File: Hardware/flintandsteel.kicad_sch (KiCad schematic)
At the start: 41 parts, among them J1 RBUS, U1 ESP32-S3, Y1 40MHz±10ppm

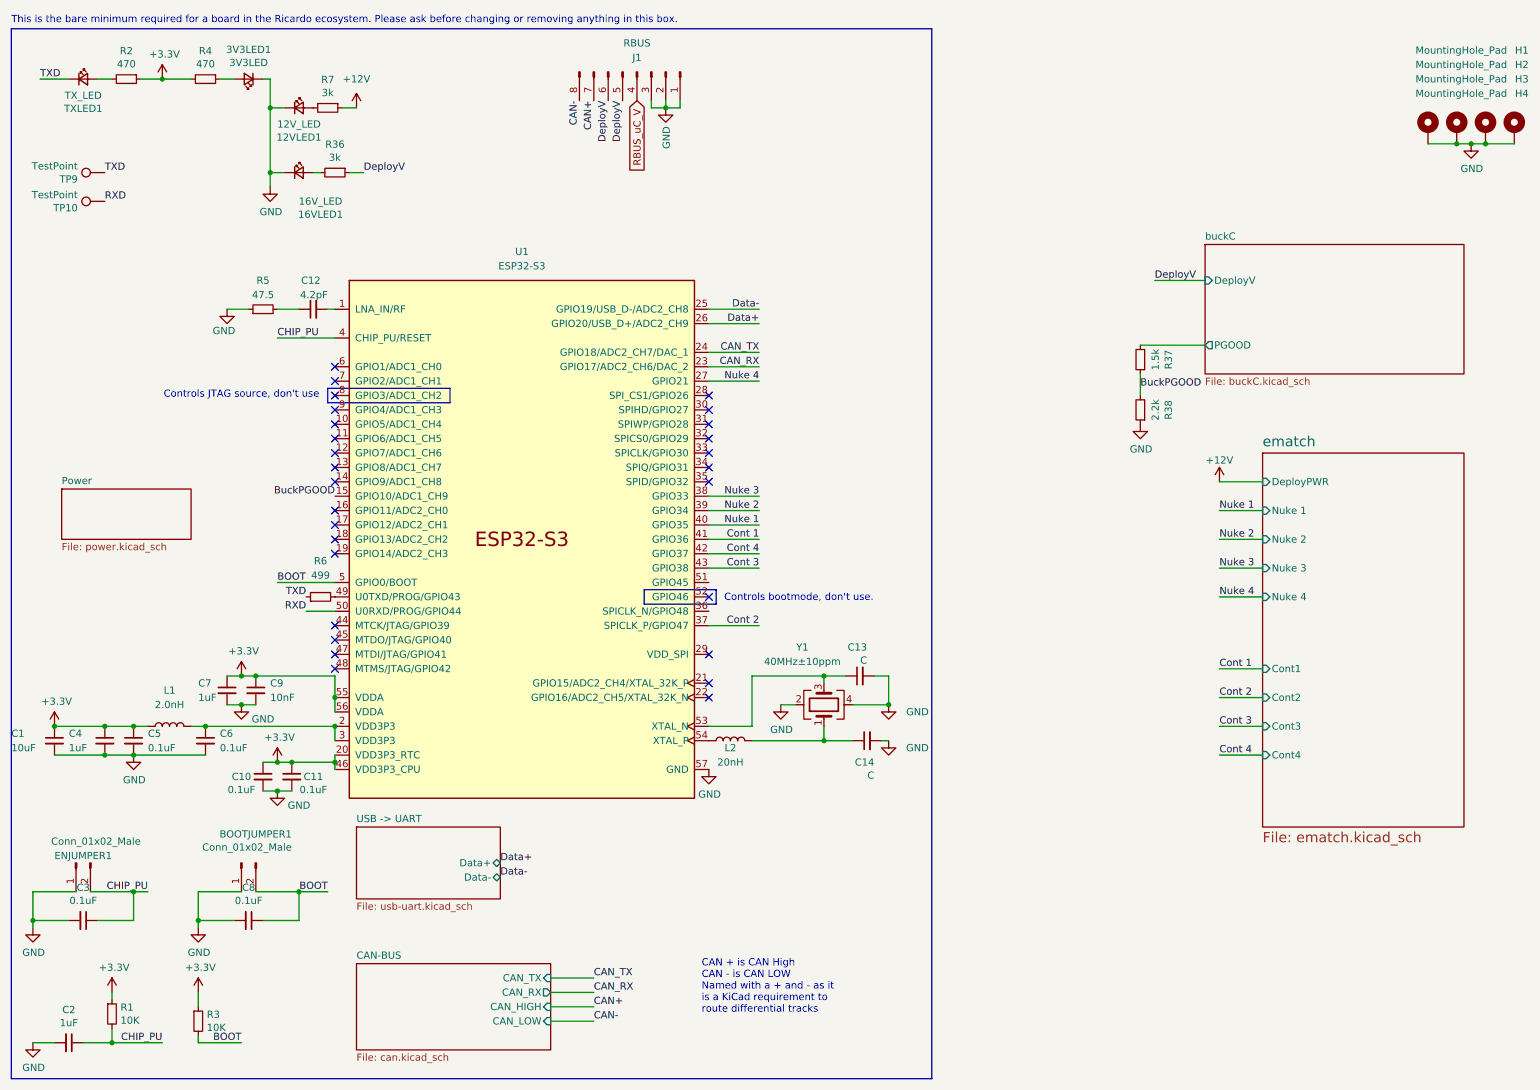
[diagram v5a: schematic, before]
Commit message: no buck, technically complete but I still want to make some changes
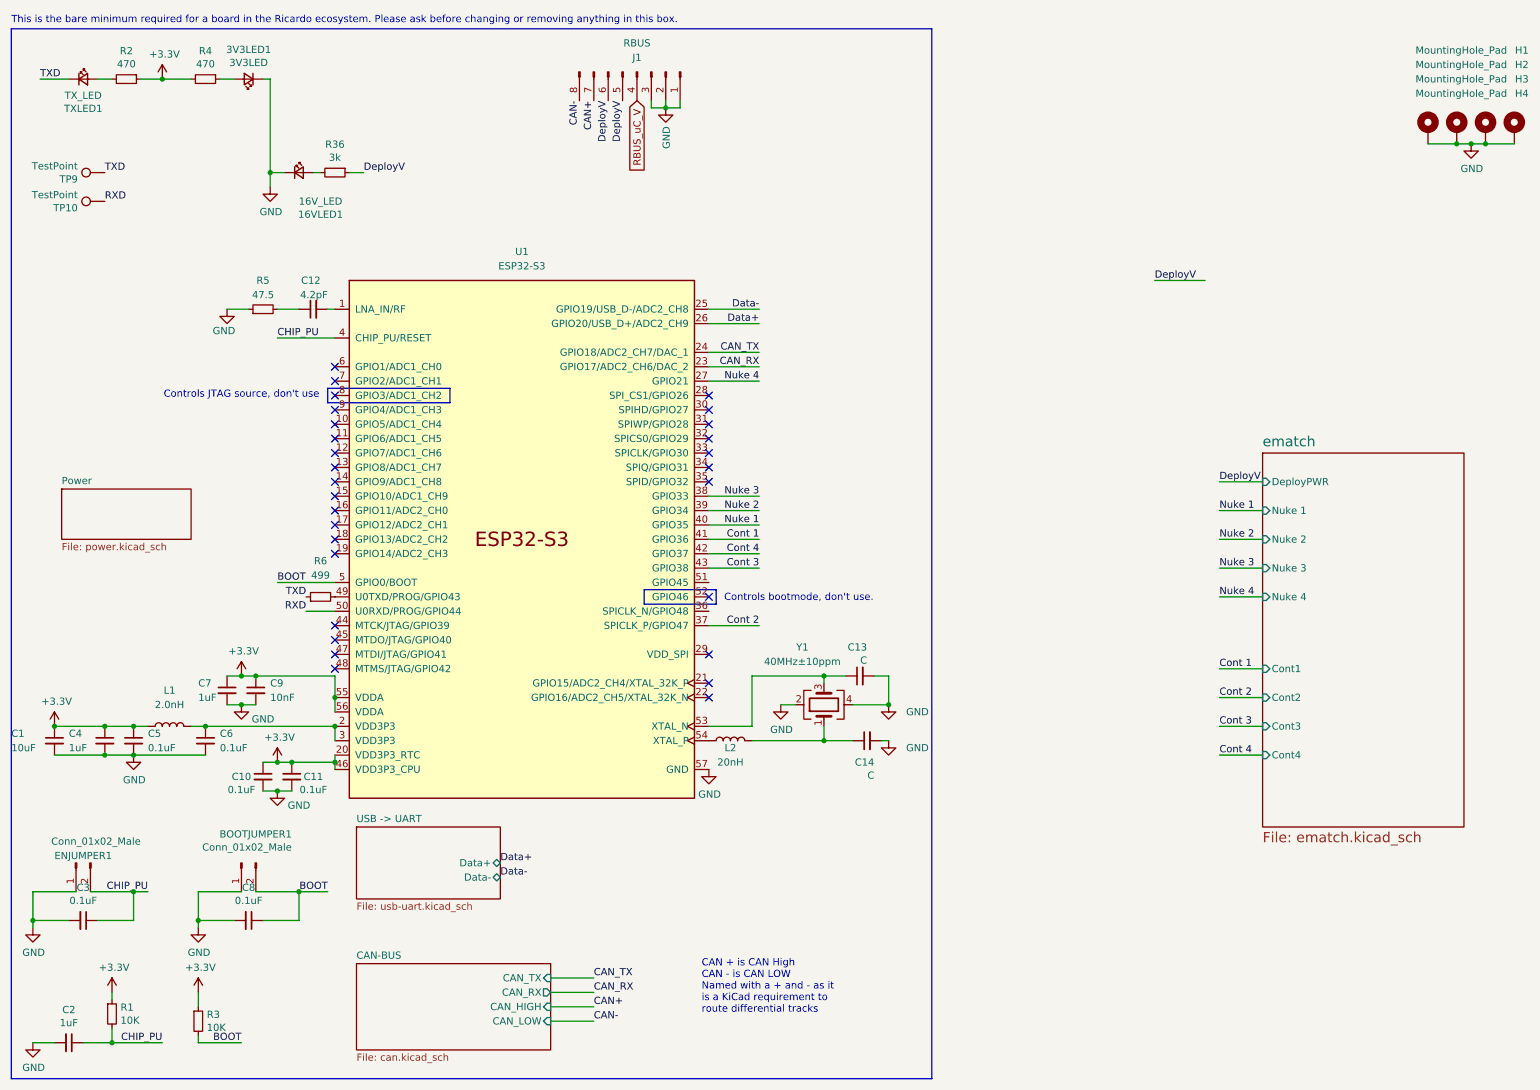
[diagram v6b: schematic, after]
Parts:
- removed 12VLED1: 12V_LED, Diode_SMD:D_0402_1005Metric, symbol Device:LED_Small
- removed R37: 1.5k, Resistor_SMD:R_0402_1005Metric, symbol Device:R_Small
- removed R38: 2.2k, Resistor_SMD:R_0402_1005Metric, symbol Device:R_Small
- removed R7: 3k, Resistor_SMD:R_0402_1005Metric, symbol Device:R_Small
- H4: footprint MountingHole:MountingHole_3.2mm_M3_DIN965_Pad -> MountingHole:MountingHole_3.2mm_M3_DIN965
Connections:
- net BuckPGOOD: no longer names the net of U1.15 (GPIO10/ADC1_CH9)
- no-connect marks 28 -> 29
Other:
- removed sheet buckC
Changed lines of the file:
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@@
   (junction (at 53.34 127) (diameter 0) (color 0 0 0 0)
-  )
-  (junction (at 58.42 26.67) (diameter 0) (color 0 0 0 0)
   )
   (junction (at 30.48 191.77) (diameter 0) (color 0 0 0 0)
@@
   (no_connect (at 69.85 77.47))
   (no_connect (at 69.85 82.55))
+  (no_connect (at 69.85 95.25))
   (no_connect (at 69.85 80.01))
   (no_connect (at 69.85 120.65))
@@
     (stroke (width 0) (type default))
   )
-  (wire (pts (xy 60.96 26.67) (xy 58.42 26.67))
-    (stroke (width 0) (type default))
-  )
   (wire (pts (xy 16.51 191.77) (xy 20.32 191.77))
     (stroke (width 0) (type default))
@@
     (stroke (width 0) (type default))
   )
-  (wire (pts (xy 212.09 73.66) (xy 212.09 77.47))
-    (stroke (width 0) (type default))
-  )
-  (wire (pts (xy 212.09 68.58) (xy 223.52 68.58))
-    (stroke (width 0) (type default))
-  )
   (wire (pts (xy 69.85 130.81) (xy 69.85 133.35))
     (stroke (width 0) (type default))
@@
     (stroke (width 0) (type default))
   )
-  (wire (pts (xy 58.42 21.59) (xy 58.42 26.67))
+  (wire (pts (xy 58.42 21.59) (xy 58.42 38.1))
     (stroke (width 0) (type default))
   )
@@
     (stroke (width 0) (type default))
   )
-  (wire (pts (xy 58.42 26.67) (xy 58.42 38.1))
-    (stroke (width 0) (type default))
-  )
   (wire (pts (xy 156.21 135.89) (xy 156.21 138.43))
     (stroke (width 0) (type default))
@@
   )
   (wire (pts (xy 53.34 127) (xy 55.88 127))
-    (stroke (width 0) (type default))
-  )
-  (wire (pts (xy 73.66 26.67) (xy 71.12 26.67))
     (stroke (width 0) (type default))
   )
@@
     (effects (font (size 1.27 1.27)) (justify left bottom))
   )
-  (label "BuckPGOOD" (at 212.09 76.2 0) (fields_autoplaced)
-    (effects (font (size 1.27 1.27)) (justify left bottom))
-  )
   (label "Nuke 2" (at 144.78 97.79 180) (fields_autoplaced)
     (effects (font (size 1.27 1.27)) (justify right bottom))
@@
     (effects (font (size 1.27 1.27)) (justify left bottom))
   )
-  (label "BuckPGOOD" (at 69.85 95.25 180) (fields_autoplaced)
-    (effects (font (size 1.27 1.27)) (justify right bottom))
-  )
   (label "TXD" (at 29.21 38.1 0) (fields_autoplaced)
     (effects (font (size 1.27 1.27)) (justify left bottom))
   )
   (label "CAN_TX" (at 115.57 180.34 0) (fields_autoplaced)
+    (effects (font (size 1.27 1.27)) (justify left bottom))
+  )
+  (label "DeployV" (at 226.06 92.71 0) (fields_autoplaced)
     (effects (font (size 1.27 1.27)) (justify left bottom))
   )
@@
     )
   )
-  (symbol (lib_id "Device:LED_Small") (at 63.5 26.67 0) (unit 1)
-    (in_bom yes) (on_board yes) (dnp no)
-    (property "Reference" "12VLED1" (at 63.5 31.877 0)
-      (effects (font (size 1.27 1.27)))
-    )
-    (property "Value" "12V_LED" (at 63.5 29.5656 0)
-      (effects (font (size 1.27 1.27)))
-    )
-    (property "Footprint" "Diode_SMD:D_0402_1005Metric" (at 63.5 26.67 90)
-      (effects (font (size 1.27 1.27)) hide)
-    )
-    (property "Datasheet" "~" (at 63.5 26.67 90)
-      (effects (font (size 1.27 1.27)) hide)
-    )
-    (pin "1")
-    (pin "2")
-    (instances
-      (project "flintandsteel"
-        (path "/7db990e4-92e1-4f99-b4d2-435bbec1ba83"
-          (reference "12VLED1") (unit 1)
-        )
-      )
-    )
-  )
-  (symbol (lib_id "Device:R_Small") (at 68.58 26.67 270) (unit 1)
-    (in_bom yes) (on_board yes) (dnp no)
-    (property "Reference" "R7" (at 68.58 21.6916 90)
-      (effects (font (size 1.27 1.27)))
-    )
-    (property "Value" "3k" (at 68.58 24.003 90)
-      (effects (font (size 1.27 1.27)))
-    )
-    (property "Footprint" "Resistor_SMD:R_0402_1005Metric" (at 68.58 26.67 0)
-      (effects (font (size 1.27 1.27)) hide)
-    )
-    (property "Datasheet" "~" (at 68.58 26.67 0)
-      (effects (font (size 1.27 1.27)) hide)
-    )
-    (pin "1")
-    (pin "2")
-    (instances
-      (project "flintandsteel"
-        (path "/7db990e4-92e1-4f99-b4d2-435bbec1ba83"
-          (reference "R7") (unit 1)
-        )
-      )
-    )
-  )
   (symbol (lib_id "Connector:TestPoint") (at 29.21 38.1 90) (unit 1)
     (in_bom yes) (on_board yes) (dnp no)
@@
     )
   )
-  (symbol (lib_id "power:+12V") (at 73.66 26.67 0) (unit 1)
-    (in_bom yes) (on_board yes) (dnp no)
-    (property "Reference" "#PWR015" (at 73.66 30.48 0)
-      (effects (font (size 1.27 1.27)) hide)
-    )
-    (property "Value" "+12V" (at 73.66 21.59 0)
-      (effects (font (size 1.27 1.27)))
-    )
-    (property "Footprint" "" (at 73.66 26.67 0)
-      (effects (font (size 1.27 1.27)) hide)
-    )
-    (property "Datasheet" "" (at 73.66 26.67 0)
-      (effects (font (size 1.27 1.27)) hide)
-    )
-    (pin "1")
-    (instances
-      (project "flintandsteel"
-        (path "/7db990e4-92e1-4f99-b4d2-435bbec1ba83"
-          (reference "#PWR015") (unit 1)
-        )
-      )
-    )
-  )
   (symbol (lib_id "Mechanical:MountingHole_Pad") (at 278.13 30.48 0) (unit 1)
     (in_bom yes) (on_board yes) (dnp no)
@@
       (effects (font (size 1.27 1.27)) (justify right))
     )
-    (property "Footprint" "MountingHole:MountingHole_3.2mm_M3_DIN965_Pad" (at 278.13 30.48 0)
+    (property "Footprint" "MountingHole:MountingHole_3.2mm_M3_DIN965" (at 278.13 30.48 0)
       (effects (font (size 1.27 1.27)) hide)
     )
@@
         (path "/7db990e4-92e1-4f99-b4d2-435bbec1ba83"
           (reference "#PWR013") (unit 1)
-        )
-      )
-    )
-  )
-  (symbol (lib_id "Device:R_Small") (at 212.09 80.01 180) (unit 1)
-    (in_bom yes) (on_board yes) (dnp no)
-    (property "Reference" "R38" (at 217.0684 80.01 90)
-      (effects (font (size 1.27 1.27)))
-    )
-    (property "Value" "2.2k" (at 214.757 80.01 90)
-      (effects (font (size 1.27 1.27)))
-    )
-    (property "Footprint" "Resistor_SMD:R_0402_1005Metric" (at 212.09 80.01 0)
-      (effects (font (size 1.27 1.27)) hide)
-    )
-    (property "Datasheet" "~" (at 212.09 80.01 0)
-      (effects (font (size 1.27 1.27)) hide)
-    )
-    (pin "1")
-    (pin "2")
-    (instances
-      (project "flintandsteel"
-        (path "/7db990e4-92e1-4f99-b4d2-435bbec1ba83"
-          (reference "R38") (unit 1)
         )
       )
@@
     )
   )
-  (symbol (lib_name "+12V_1") (lib_id "power:+12V") (at 226.06 92.71 0) (unit 1)
-    (in_bom yes) (on_board yes) (dnp no) (fields_autoplaced)
-    (property "Reference" "#PWR067" (at 226.06 96.52 0)
-      (effects (font (size 1.27 1.27)) hide)
-    )
-    (property "Value" "+12V" (at 226.06 88.9 0)
-      (effects (font (size 1.27 1.27)))
-    )
-    (property "Footprint" "" (at 226.06 92.71 0)
-      (effects (font (size 1.27 1.27)) hide)
-    )
-    (property "Datasheet" "" (at 226.06 92.71 0)
-      (effects (font (size 1.27 1.27)) hide)
-    )
-    (pin "1")
-    (instances
-      (project "flintandsteel"
-        (path "/7db990e4-92e1-4f99-b4d2-435bbec1ba83"
-          (reference "#PWR067") (unit 1)
-        )
-      )
-    )
-  )
   (symbol (lib_id "power:GND") (at 270.51 33.02 0) (unit 1)
     (in_bom yes) (on_board yes) (dnp no)
@@
         (path "/7db990e4-92e1-4f99-b4d2-435bbec1ba83"
           (reference "R5") (unit 1)
-        )
-      )
-    )
-  )
-  (symbol (lib_id "Device:R_Small") (at 212.09 71.12 180) (unit 1)
-    (in_bom yes) (on_board yes) (dnp no)
-    (property "Reference" "R37" (at 217.0684 71.12 90)
-      (effects (font (size 1.27 1.27)))
-    )
-    (property "Value" "1.5k" (at 214.757 71.12 90)
-      (effects (font (size 1.27 1.27)))
-    )
-    (property "Footprint" "Resistor_SMD:R_0402_1005Metric" (at 212.09 71.12 0)
-      (effects (font (size 1.27 1.27)) hide)
-    )
-    (property "Datasheet" "~" (at 212.09 71.12 0)
-      (effects (font (size 1.27 1.27)) hide)
-    )
-    (pin "1")
-    (pin "2")
-    (instances
-      (project "flintandsteel"
-        (path "/7db990e4-92e1-4f99-b4d2-435bbec1ba83"
-          (reference "R37") (unit 1)
-        )
-      )
-    )
-  )
-  (symbol (lib_id "power:GND") (at 212.09 82.55 0) (unit 1)
-    (in_bom yes) (on_board yes) (dnp no)
-    (property "Reference" "#PWR046" (at 212.09 88.9 0)
-      (effects (font (size 1.27 1.27)) hide)
-    )
-    (property "Value" "GND" (at 212.217 86.9442 0)
-      (effects (font (size 1.27 1.27)))
-    )
-    (property "Footprint" "" (at 212.09 82.55 0)
-      (effects (font (size 1.27 1.27)) hide)
-    )
-    (property "Datasheet" "" (at 212.09 82.55 0)
-      (effects (font (size 1.27 1.27)) hide)
-    )
-    (pin "1")
-    (instances
-      (project "flintandsteel"
-        (path "/7db990e4-92e1-4f99-b4d2-435bbec1ba83"
-          (reference "#PWR046") (unit 1)
         )
       )
@@
       )
     )
-  )
-  (sheet (at 223.52 50.8) (size 45.72 22.86) (fields_autoplaced)
-    (stroke (width 0.1524) (type solid))
-    (fill (color 0 0 0 0.0000))
-    (property "Sheetname" "buckC" (at 223.52 50.0884 0)
-      (effects (font (size 1.27 1.27)) (justify left bottom))
-    )
-    (property "Sheetfile" "buckC.kicad_sch" (at 223.52 74.2446 0)
-      (effects (font (size 1.27 1.27)) (justify left top))
-    )
-    (pin "DeployV" input (at 223.52 57.15 180)
-      (effects (font (size 1.27 1.27)) (justify left))
-    )
-    (pin "PGOOD" output (at 223.52 68.58 180)
-      (effects (font (size 1.27 1.27)) (justify left))
-    )
-    (instances
-      (project "flintandsteel"
-        (path "/7db990e4-92e1-4f99-b4d2-435bbec1ba83" (page "6"))
-      )
-    )
